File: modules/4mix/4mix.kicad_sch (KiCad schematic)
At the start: 75 parts, among them U1 MCP6002-xSN, U2 MCP6002-xSN, U3 MCP6002-xSN, U4 MCP6002-xSN, U5 MCP6002-xSN, U6 MCP6002-xSN

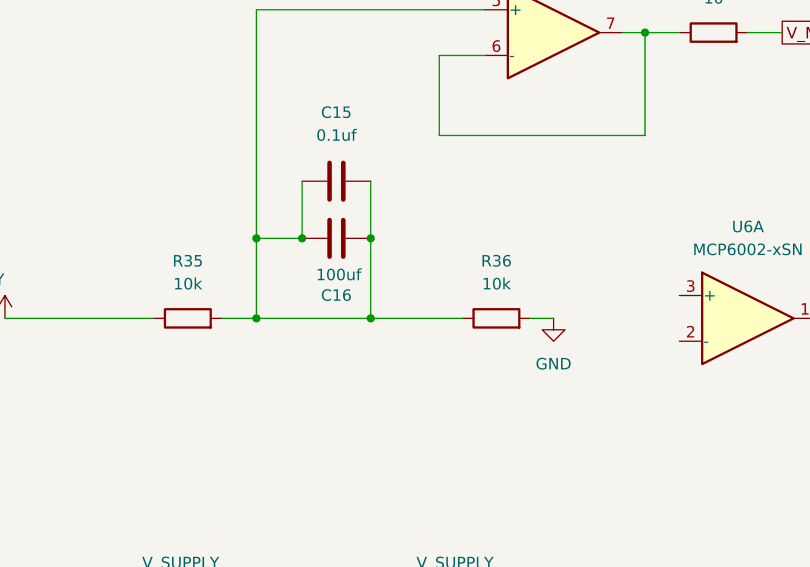
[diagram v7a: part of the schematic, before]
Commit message: Add vmid routing
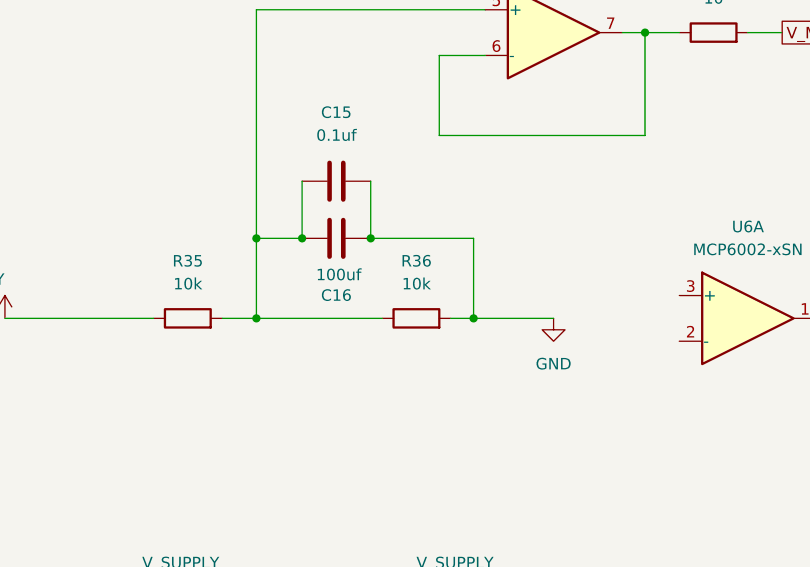
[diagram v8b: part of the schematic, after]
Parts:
- C15: footprint Capacitor_SMD:C_1206_3216Metric -> Capacitor_SMD:C_0402_1005Metric
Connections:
- net GND: now also C15.2, C16.2
- net at C15.1, C16.1, R35.2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: no longer C15.2, C16.2
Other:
- moved on the sheet: R36
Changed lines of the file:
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@@
 	)
 	(junction
-		(at 505.46 181.61)
+		(at 525.78 137.16)
 		(diameter 0)
 		(color 0 0 0 0)
 	)
 	(junction
-		(at 518.16 137.16)
+		(at 505.46 181.61)
 		(diameter 0)
 		(color 0 0 0 0)
 	)
 	(junction
-		(at 494.03 39.37)
+		(at 518.16 137.16)
 		(diameter 0)
 		(color 0 0 0 0)
 	)
 	(junction
-		(at 525.78 137.16)
+		(at 494.03 39.37)
 		(diameter 0)
 		(color 0 0 0 0)
@@
 	)
 	(junction
+		(at 537.21 146.05)
+		(diameter 0)
+		(color 0 0 0 0)
+	)
+	(junction
 		(at 535.94 39.37)
 		(diameter 0)
@@
 	)
 	(junction
-		(at 525.78 146.05)
-		(diameter 0)
-		(color 0 0 0 0)
-	)
-	(junction
 		(at 64.77 383.54)
 		(diameter 0)
@@
 	(wire
 		(pts
+			(xy 537.21 137.16) (xy 537.21 146.05)
+		)
+		(stroke
+			(width 0)
+			(type default)
+		)
+	)
+	(wire
+		(pts
 			(xy 554.99 38.1) (xy 557.53 38.1)
 		)
@@
 	(wire
 		(pts
+			(xy 525.78 130.81) (xy 525.78 137.16)
+		)
+		(stroke
+			(width 0)
+			(type default)
+		)
+	)
+	(wire
+		(pts
 			(xy 513.08 201.93) (xy 505.46 201.93)
 		)
@@
 	(wire
 		(pts
-			(xy 513.08 146.05) (xy 525.78 146.05)
+			(xy 513.08 146.05) (xy 527.05 146.05)
 		)
 		(stroke
@@
 	(wire
 		(pts
-			(xy 525.78 137.16) (xy 525.78 146.05)
-		)
-		(stroke
-			(width 0)
-			(type default)
-		)
-	)
-	(wire
-		(pts
 			(xy 85.09 121.92) (xy 85.09 138.43)
 		)
@@
 	(wire
 		(pts
-			(xy 546.1 146.05) (xy 543.56 146.05)
+			(xy 546.1 146.05) (xy 537.21 146.05)
 		)
 		(stroke
@@
 	(wire
 		(pts
-			(xy 525.78 146.05) (xy 535.94 146.05)
-		)
-		(stroke
-			(width 0)
-			(type default)
-		)
-	)
-	(wire
-		(pts
 			(xy 374.65 53.34) (xy 374.65 45.72)
 		)
@@
 	(wire
 		(pts
+			(xy 525.78 137.16) (xy 537.21 137.16)
+		)
+		(stroke
+			(width 0)
+			(type default)
+		)
+	)
+	(wire
+		(pts
 			(xy 267.97 171.45) (xy 273.05 171.45)
 		)
@@
 	(wire
 		(pts
-			(xy 525.78 130.81) (xy 525.78 137.16)
-		)
-		(stroke
-			(width 0)
-			(type default)
-		)
-	)
-	(wire
-		(pts
 			(xy 284.48 81.28) (xy 284.48 69.85)
 		)
@@
 	(wire
 		(pts
+			(xy 537.21 146.05) (xy 534.67 146.05)
+		)
+		(stroke
+			(width 0)
+			(type default)
+		)
+	)
+	(wire
+		(pts
 			(xy 228.6 304.8) (xy 228.6 320.04)
 		)
@@
 			)
 		)
-		(property "Footprint" "Capacitor_SMD:C_1206_3216Metric"
+		(property "Footprint" "Capacitor_SMD:C_0402_1005Metric"
 			(at 525.78 129.8448 0)
 			(effects
@@
 	(symbol
 		(lib_id "Device:R")
-		(at 539.75 146.05 90)
+		(at 530.86 146.05 90)
 		(unit 1)
 		(exclude_from_sim no)
@@
 		(fields_autoplaced yes)
 		(property "Reference" "R36"
-			(at 539.75 139.7 90)
+			(at 530.86 139.7 90)
 			(effects
 				(font
@@
 		)
 		(property "Value" "10k"
-			(at 539.75 142.24 90)
+			(at 530.86 142.24 90)
 			(effects
 				(font
@@
 		)
 		(property "Footprint" "Resistor_SMD:R_0402_1005Metric"
-			(at 539.75 147.828 90)
+			(at 530.86 147.828 90)
 			(effects
 				(font
@@
 		)
 		(property "Datasheet" "~"
-			(at 539.75 146.05 0)
+			(at 530.86 146.05 0)
 			(effects
 				(font
@@
 		)
 		(property "Description" "Resistor"
-			(at 539.75 146.05 0)
+			(at 530.86 146.05 0)
 			(effects
 				(font
